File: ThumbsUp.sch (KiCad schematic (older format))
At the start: 159 parts, among them J19 52559-1233, J32 Battery, SW2 SW_DIP_x01, U1 ProMicro

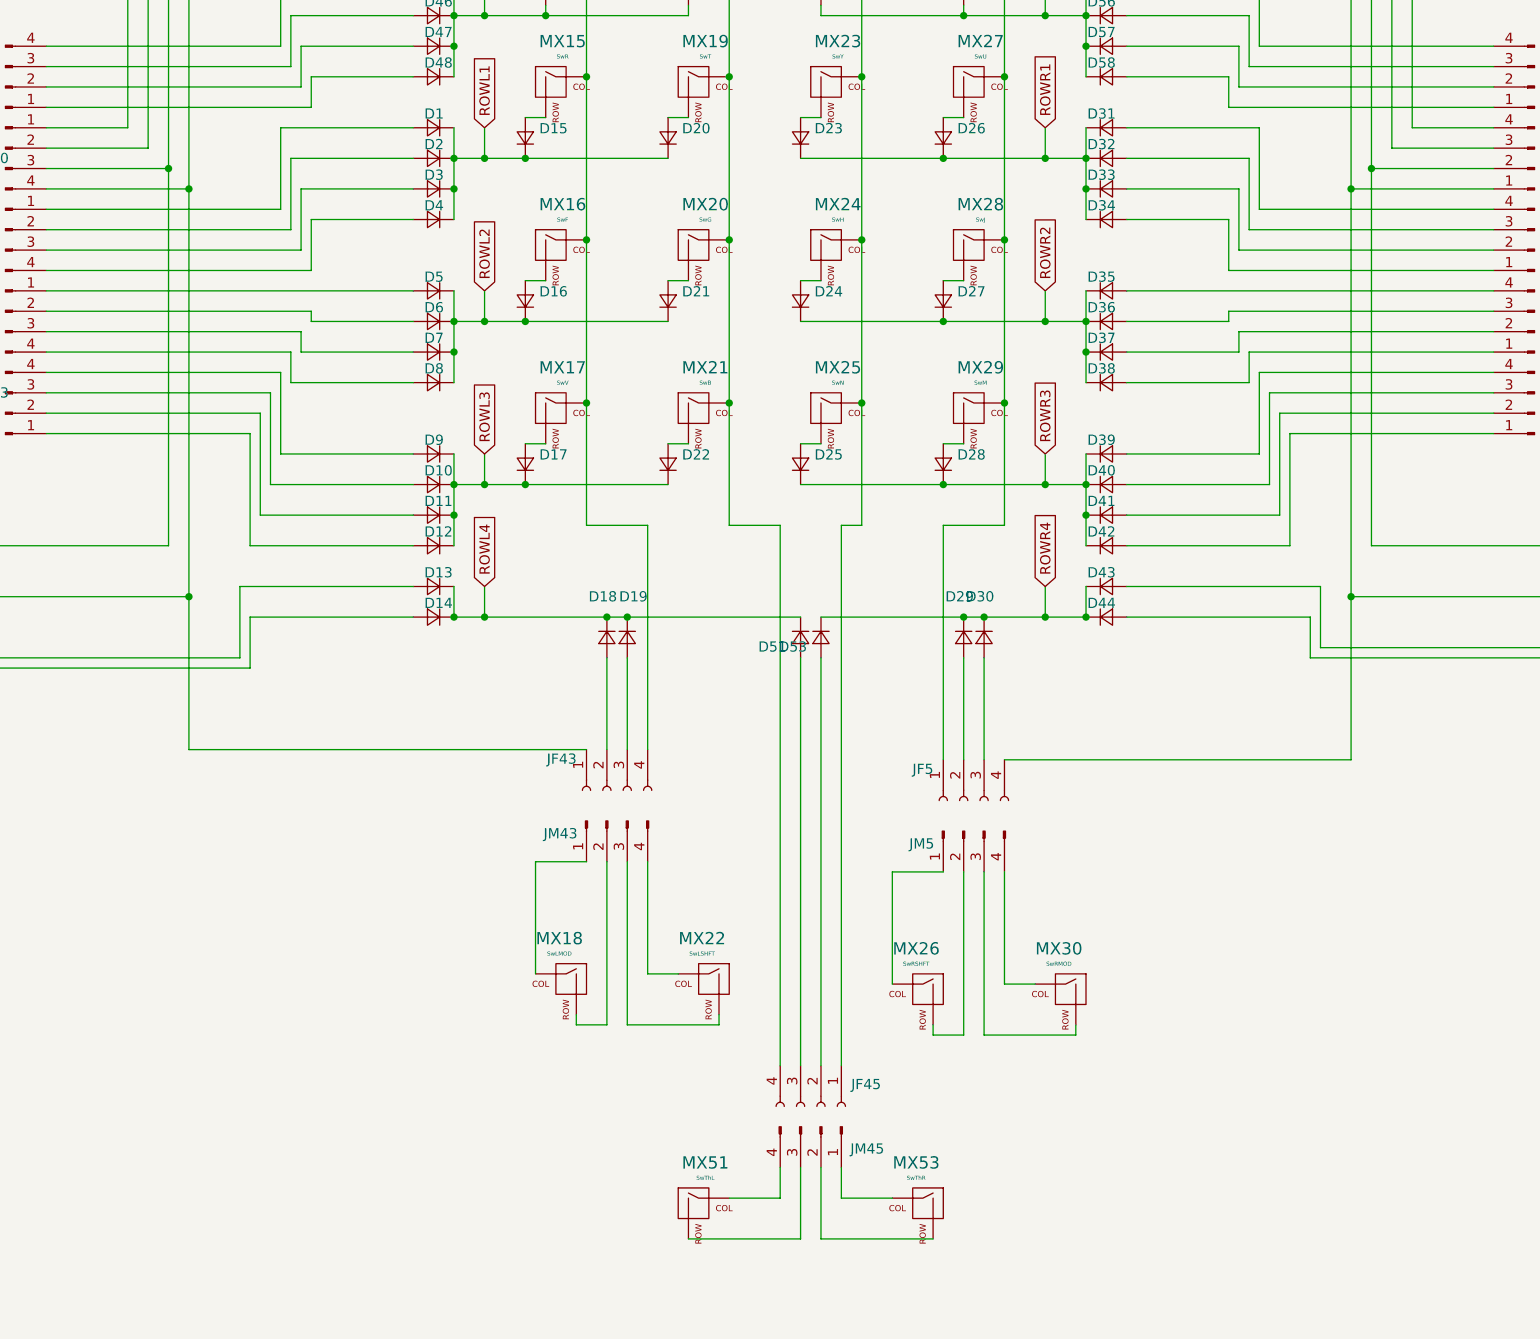
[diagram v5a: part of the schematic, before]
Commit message: Fixed the thumbcluster connections.
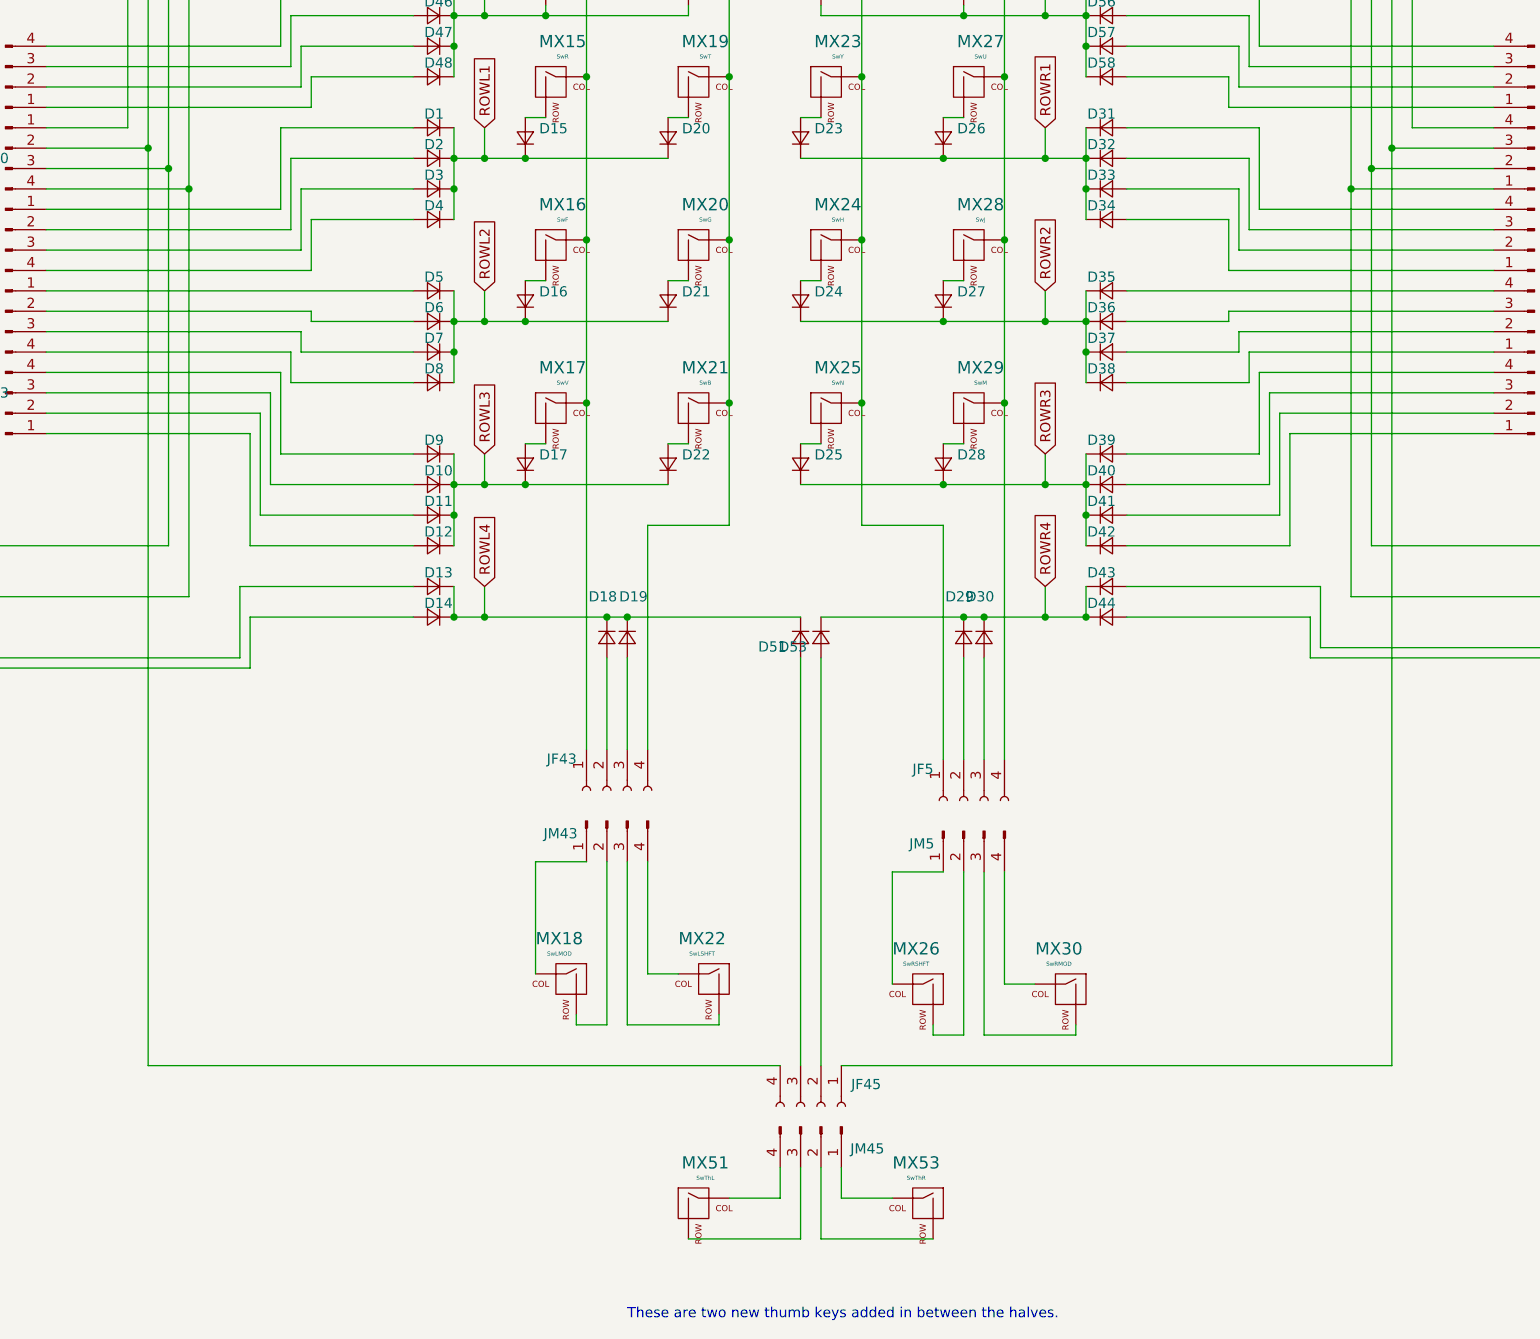
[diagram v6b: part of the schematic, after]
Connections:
- net COL1: now also JF45.1 (Pin_1), JF45.4 (Pin_4)
- net COL3: no longer JF43.1 (Pin_1), JF5.4 (Pin_4)
- net COL4: now also JF43.1 (Pin_1), JF5.4 (Pin_4); no longer JF43.4 (Pin_4), JF5.1 (Pin_1)
- net COL5: now also JF43.4 (Pin_4), JF5.1 (Pin_1); no longer JF45.1 (Pin_1), JF45.4 (Pin_4)
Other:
- note added: "These are two new thumb keys added in between the halves."
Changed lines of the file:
@@
 	10000 10450 9750 10450
-$Comp
-L Connector:Conn_01x04_Female JF5
-U 1 1 62A1D5D4
-P 10100 10100
-F 0 "JF5" V 9946 10248 50  0000 L CNN
-F 1 "Conn_01x04_Female" V 10050 9100 50  0001 L CNN
-F 2 "Connector_PinSocket_2.54mm:PinSocket_1x04_P2.54mm_Vertical" H 10100 10100 50  0001 C CNN
-F 3 "~" H 10100 10100 50  0001 C CNN
-	1    10100 10100
-	0    -1   1    0
-$EndComp
 $Comp
 L Connector:Conn_01x04_Female JF3
@@
 	9300 9200 8450 9200
 Connection ~ 8450 9200
-Wire Wire Line
-	10000 8750 10300 8750
-Wire Wire Line
-	10300 8750 10300 8150
 Connection ~ 10300 8150
-Wire Wire Line
-	9500 11400 9500 8750
-Wire Wire Line
-	9500 8750 9600 8750
-Wire Wire Line
-	9200 11400 9200 8750
-Wire Wire Line
-	9200 8750 8950 8750
-Wire Wire Line
-	8550 8750 8250 8750
-Wire Wire Line
-	8250 8750 8250 8150
 Connection ~ 8250 8150
-Wire Wire Line
-	8250 9850 6300 9850
-Wire Wire Line
-	6300 9850 6300 9100
-Connection ~ 6300 9100
-Wire Wire Line
-	10300 9900 12000 9900
-Wire Wire Line
-	12000 9900 12000 9100
-Connection ~ 12000 9100
 Wire Wire Line
 	9500 11900 9500 12050
@@
 Wire Wire Line
 	2850 10850 3200 10850
+Wire Wire Line
+	9600 8750 10000 8750
+Wire Wire Line
+	10300 8150 10300 9900
+Wire Wire Line
+	8250 8150 8250 9850
+Wire Wire Line
+	8550 8750 8950 8750
+Wire Wire Line
+	9500 11400 12200 11400
+Wire Wire Line
+	12200 11400 12200 6900
+Connection ~ 12200 6900
+Wire Wire Line
+	9200 11400 6100 11400
+Wire Wire Line
+	6100 11400 6100 6900
+Connection ~ 6100 6900
+Text Notes 8450 12650 0    50   ~ 0
+These are two new thumb keys added in between the halves.
+$Comp
+L Connector:Conn_01x04_Female JF5
+U 1 1 62A1D5D4
+P 10100 10100
+F 0 "JF5" V 9946 10248 50  0000 L CNN
+F 1 "Conn_01x04_Female" V 10050 9100 50  0001 L CNN
+F 2 "Connector_PinSocket_2.54mm:PinSocket_1x04_P2.54mm_Vertical" H 10100 10100 50  0001 C CNN
+F 3 "~" H 10100 10100 50  0001 C CNN
+	1    10100 10100
+	0    -1   1    0
+$EndComp
 $EndSCHEMATC

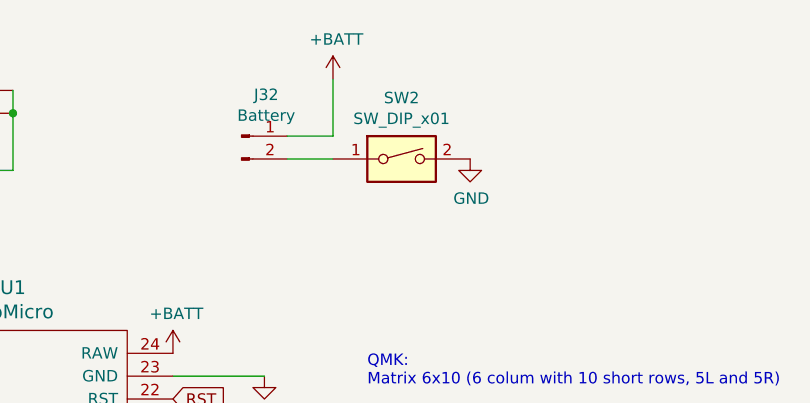
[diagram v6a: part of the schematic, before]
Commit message: Moved power switch to the positive line. Re-added silkscreens.
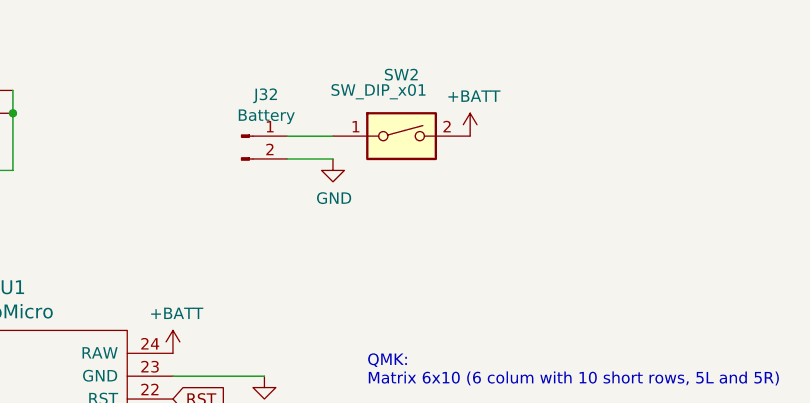
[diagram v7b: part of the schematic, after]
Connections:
- net +BATT: now also SW2.2; no longer J32.1 (Pin_1)
- net GND: now also J32.2 (Pin_2); no longer SW2.2
- net at SW2.1: now also J32.1 (Pin_1); no longer J32.2 (Pin_2)
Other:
- moved on the sheet: SW2
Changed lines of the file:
@@
 L Switch:SW_DIP_x01 SW2
 U 1 1 63C62925
-P 5300 1400
-F 0 "SW2" H 5300 1667 50  0000 C CNN
-F 1 "SW_DIP_x01" H 5300 1576 50  0000 C CNN
-F 2 "1825232-1:18252321" H 5300 1400 50  0001 C CNN
-F 3 "~" H 5300 1400 50  0001 C CNN
-	1    5300 1400
+P 5300 1300
+F 0 "SW2" H 5300 1567 50  0000 C CNN
+F 1 "SW_DIP_x01" H 5200 1500 50  0000 C CNN
+F 2 "1825232-1:18252321" H 5300 1300 50  0001 C CNN
+F 3 "~" H 5300 1300 50  0001 C CNN
+	1    5300 1300
 	1    0    0    -1
 $EndComp
@@
 	4800 1300 5000 1300
 Wire Wire Line
-	5000 1300 5000 1050
-Wire Wire Line
 	4800 1400 5000 1400
 $Comp
 L power:GND #PWR0108
 U 1 1 63CAF318
-P 5600 1400
-F 0 "#PWR0108" H 5600 1150 50  0001 C CNN
-F 1 "GND" H 5605 1227 50  0000 C CNN
-F 2 "" H 5600 1400 50  0001 C CNN
-F 3 "" H 5600 1400 50  0001 C CNN
-	1    5600 1400
+P 5000 1400
+F 0 "#PWR0108" H 5000 1150 50  0001 C CNN
+F 1 "GND" H 5005 1227 50  0000 C CNN
+F 2 "" H 5000 1400 50  0001 C CNN
+F 3 "" H 5000 1400 50  0001 C CNN
+	1    5000 1400
 	1    0    0    -1
 $EndComp
@@
 L power:+BATT #PWR0109
 U 1 1 63D45784
-P 5000 1050
-F 0 "#PWR0109" H 5000 900 50  0001 C CNN
-F 1 "+BATT" H 5015 1223 50  0000 C CNN
-F 2 "" H 5000 1050 50  0001 C CNN
-F 3 "" H 5000 1050 50  0001 C CNN
-	1    5000 1050
+P 5600 1300
+F 0 "#PWR0109" H 5600 1150 50  0001 C CNN
+F 1 "+BATT" H 5615 1473 50  0000 C CNN
+F 2 "" H 5600 1300 50  0001 C CNN
+F 3 "" H 5600 1300 50  0001 C CNN
+	1    5600 1300
 	1    0    0    -1
 $EndComp
